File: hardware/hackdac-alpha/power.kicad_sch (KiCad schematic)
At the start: 51 parts, among them J10 HOLE, J11 HOLE, J12 HOLE, J13 HOLE, J6 EXT LEDS, J7 EXT POWER, J8 HOLE, J9 HOLE, P3 P28, P4 P20, Q7 IRLML2244, U10 74LVC1G07, U11 TPS61170DRVR, U12 TPS63700DRCT, U3 TLE2082

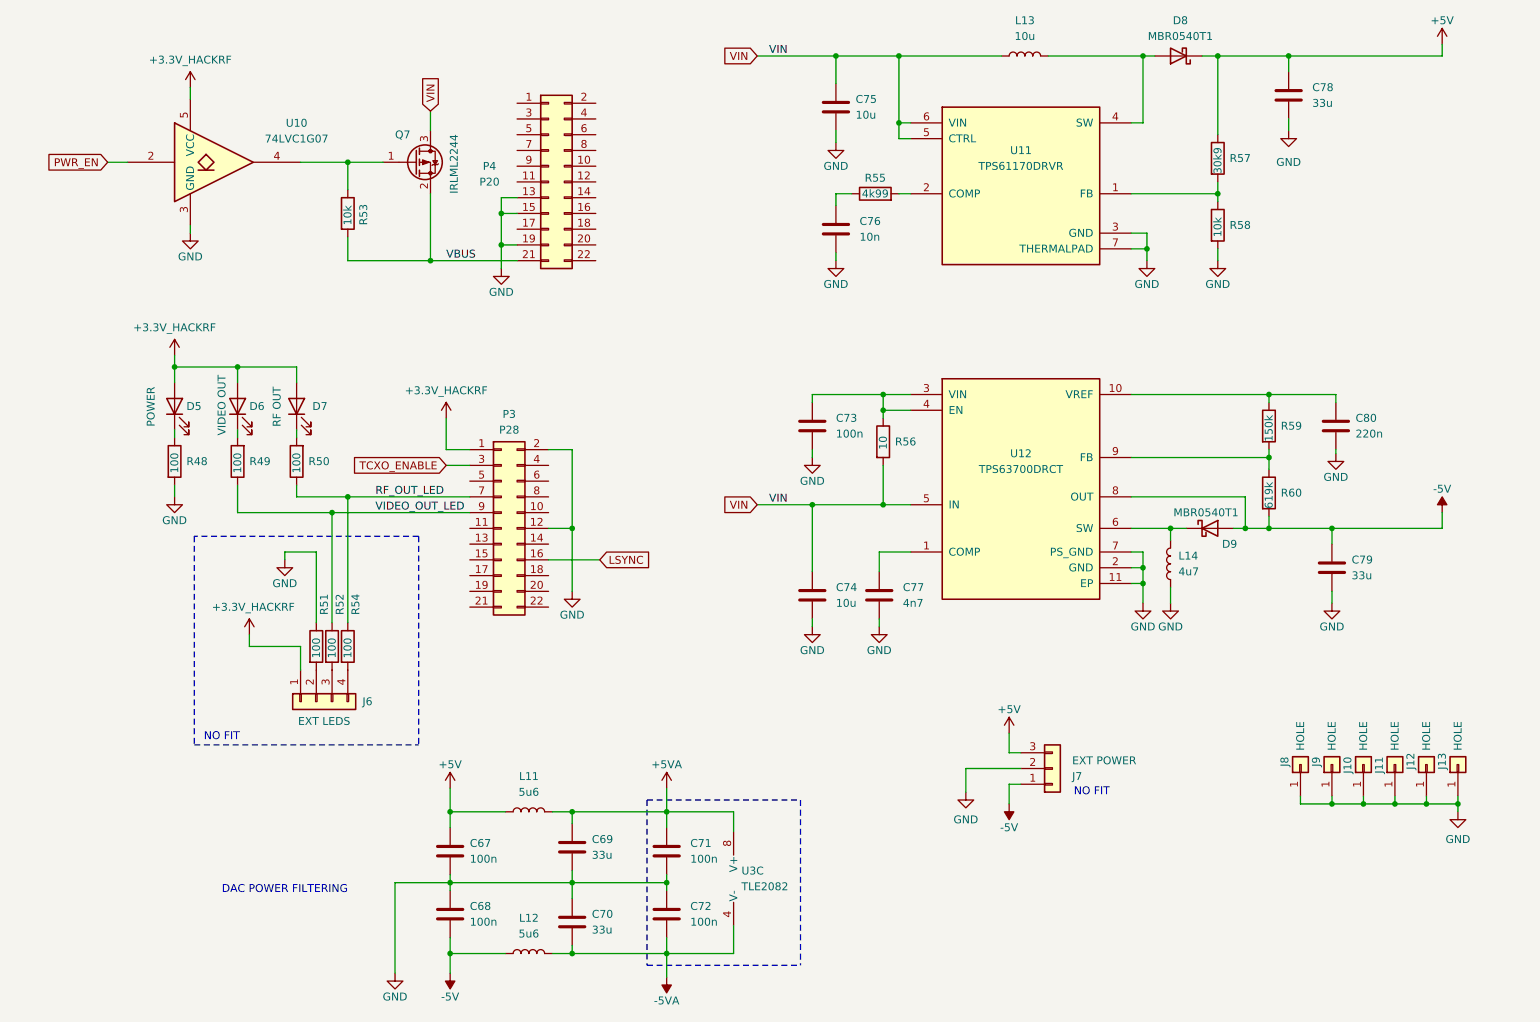
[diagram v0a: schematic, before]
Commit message: Modify I2C buffering to allow power-down of HackDAC
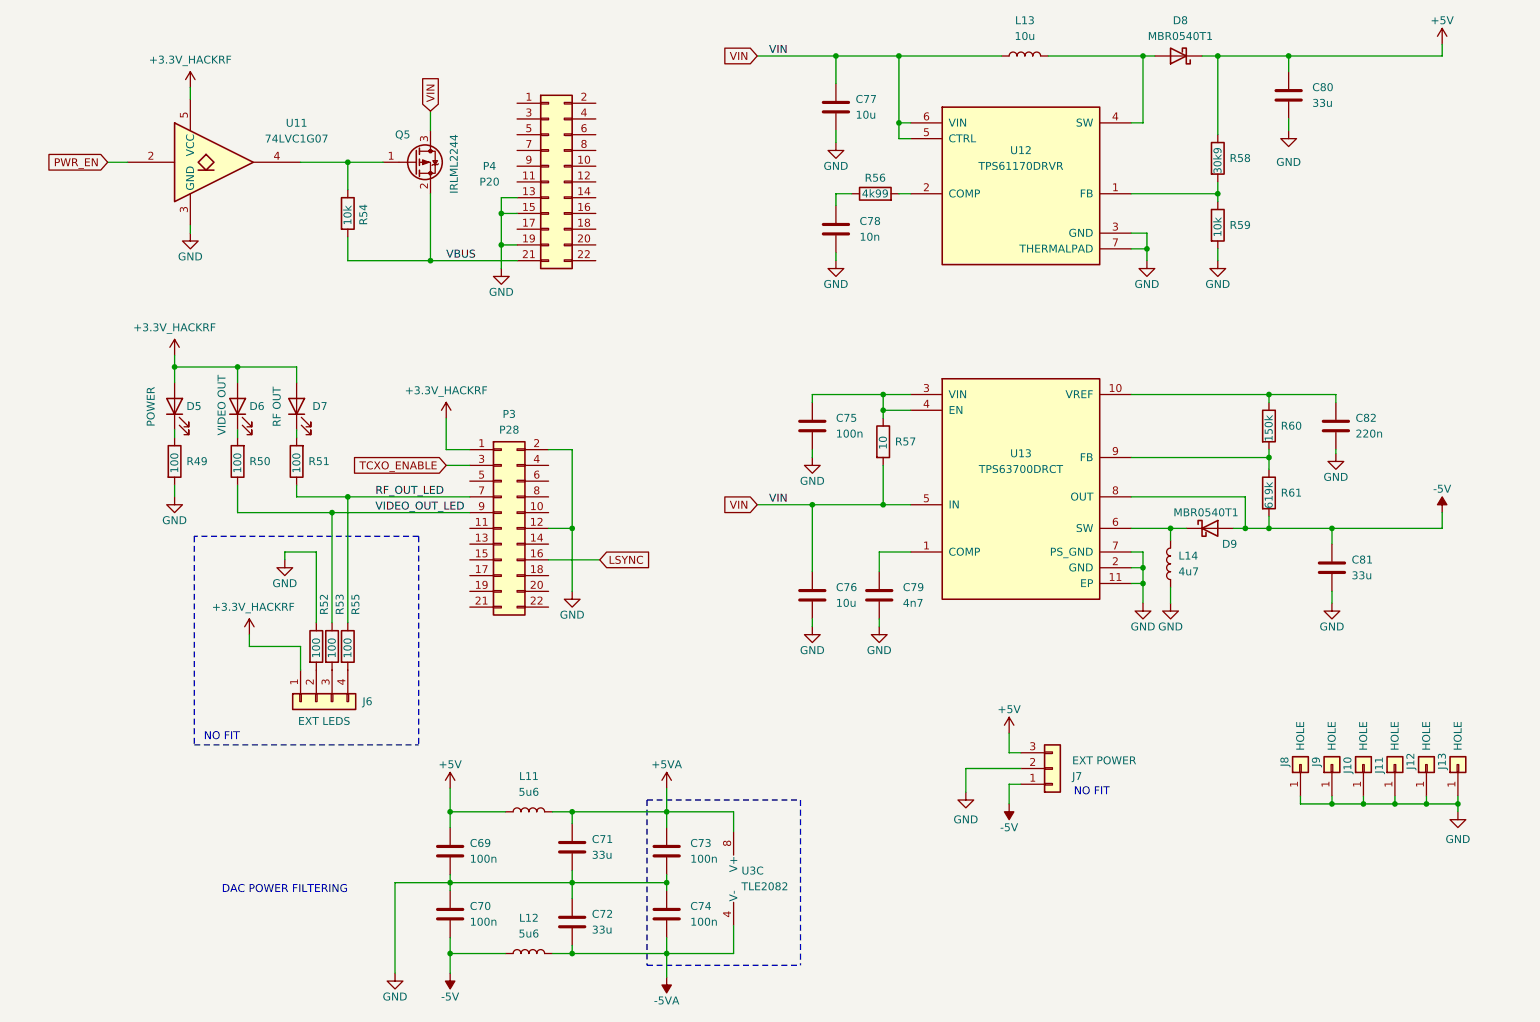
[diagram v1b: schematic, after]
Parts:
- renumbered C67 to C69, C68 to C70, C69 to C71, C70 to C72, C71 to C73, C72 to C74, C73 to C75, C74 to C76, C75 to C77, C76 to C78, C77 to C79, C78 to C80, C79 to C81, C80 to C82, Q7 to Q5, R48 to R49, R49 to R50, R50 to R51, R51 to R52, R52 to R53, R53 to R54, R54 to R55, R55 to R56, R56 to R57, R57 to R58, R58 to R59, R59 to R60, R60 to R61, U10 to U11, U11 to U12, U12 to U13

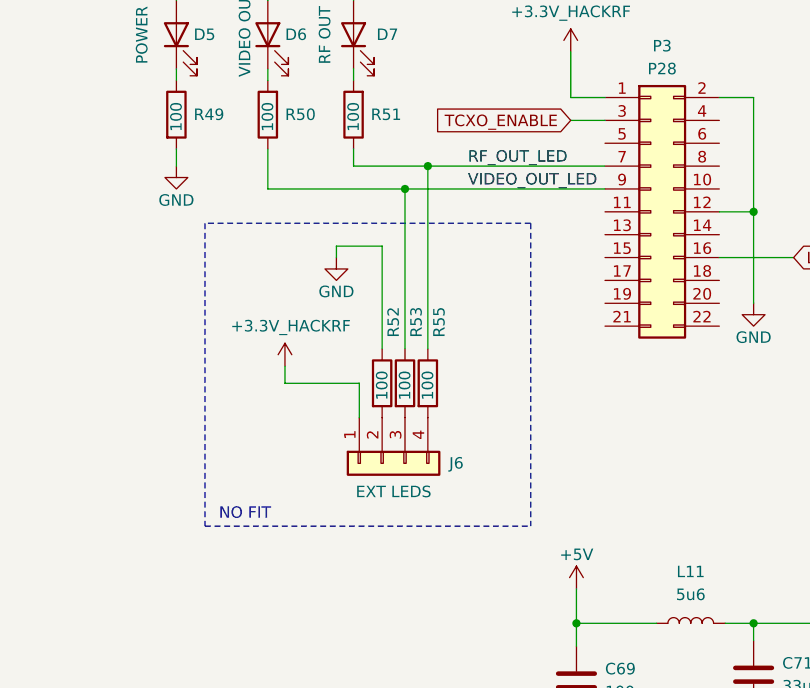
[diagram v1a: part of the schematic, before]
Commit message: Move LEDs underneath lightpipes
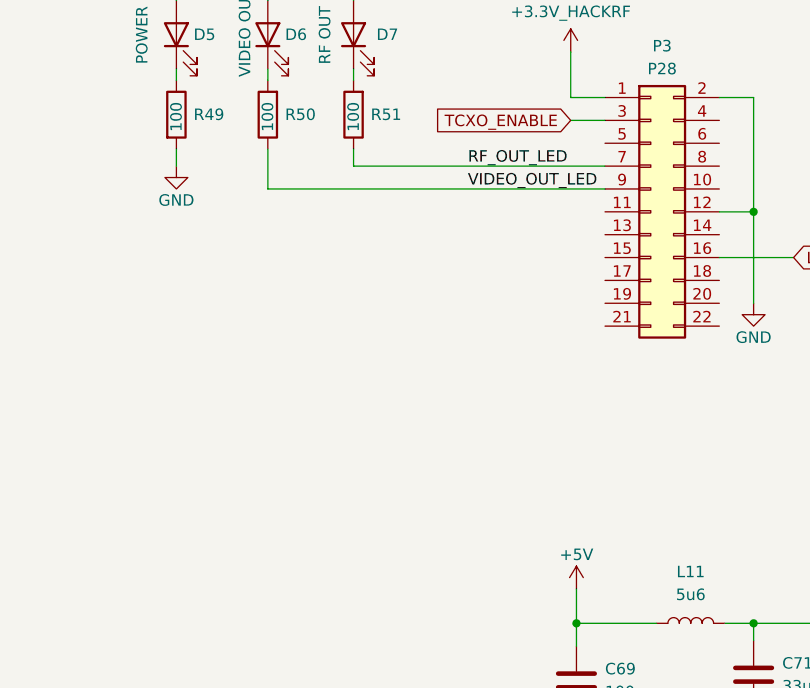
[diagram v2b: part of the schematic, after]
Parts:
- removed J6: EXT LEDS, Connector_Molex:Molex_PicoBlade_53047-0410_1x04_P1.25mm_Vertical, symbol Connector_Generic:Conn_01x04
- removed R52, R53, R55: 100, Resistor_SMD:R_0603_1608Metric, symbol Device:R

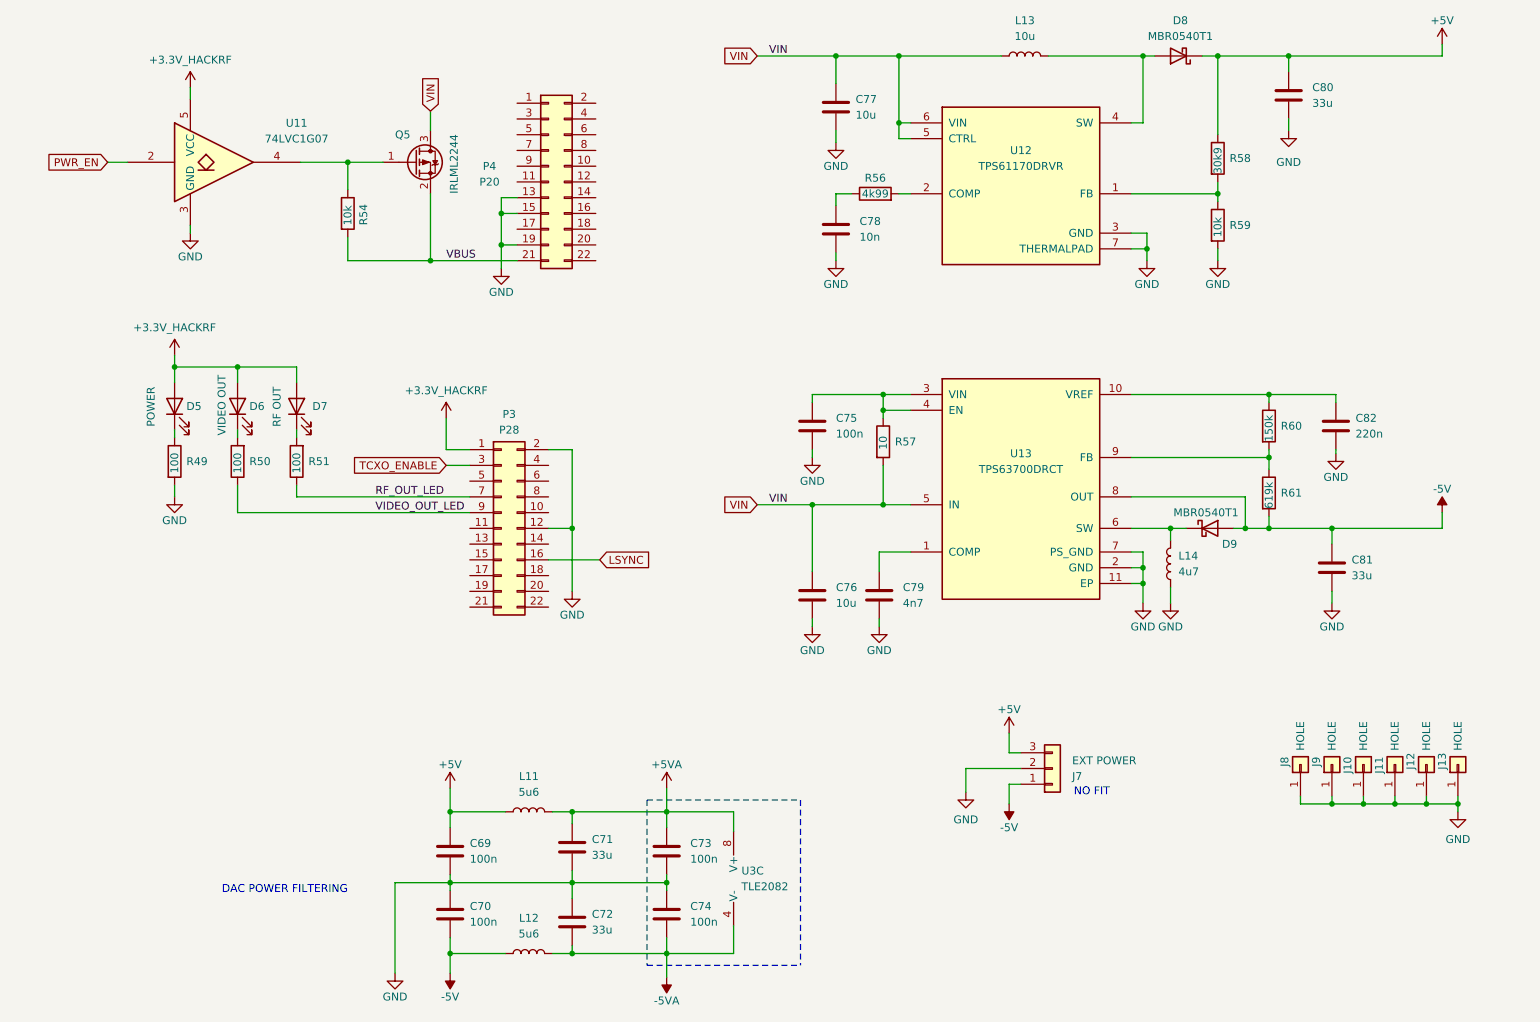
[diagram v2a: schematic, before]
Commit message: Add jumper to configure sync out connector
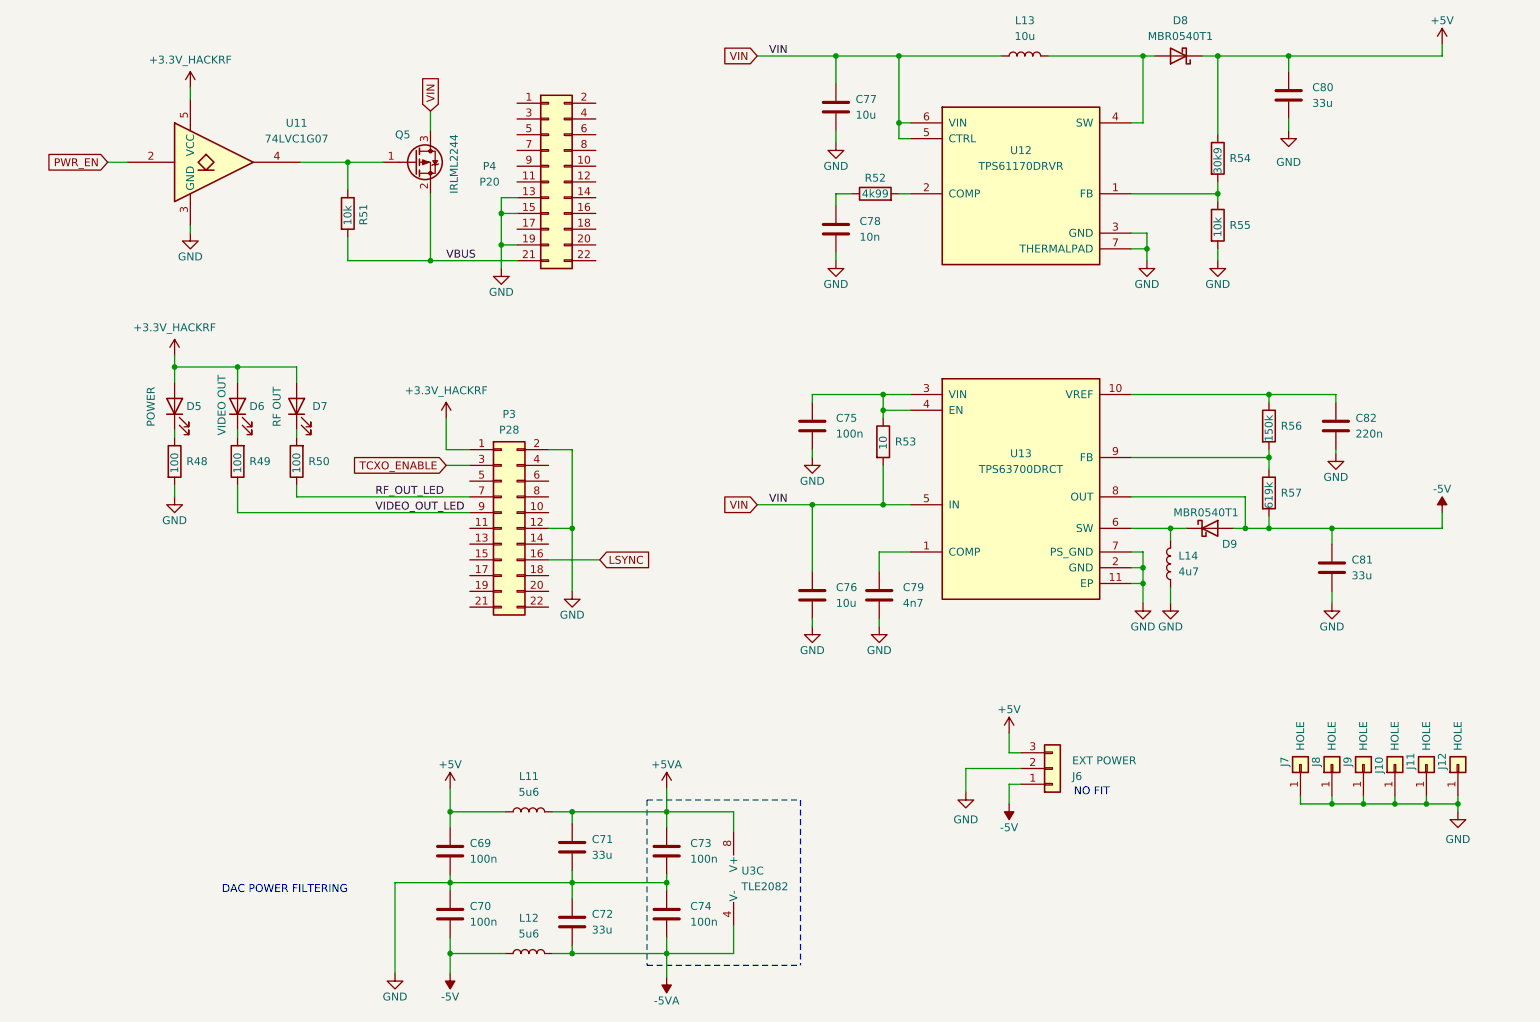
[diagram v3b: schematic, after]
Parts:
- renumbered J11 to J10, J12 to J11, J13 to J12, J7 to J6, J8 to J7, J9 to J8, J10 to J9, R49 to R48, R50 to R49, R51 to R50, R54 to R51, R56 to R52, R57 to R53, R58 to R54, R59 to R55, R60 to R56, R61 to R57

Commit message: Added configuration straps
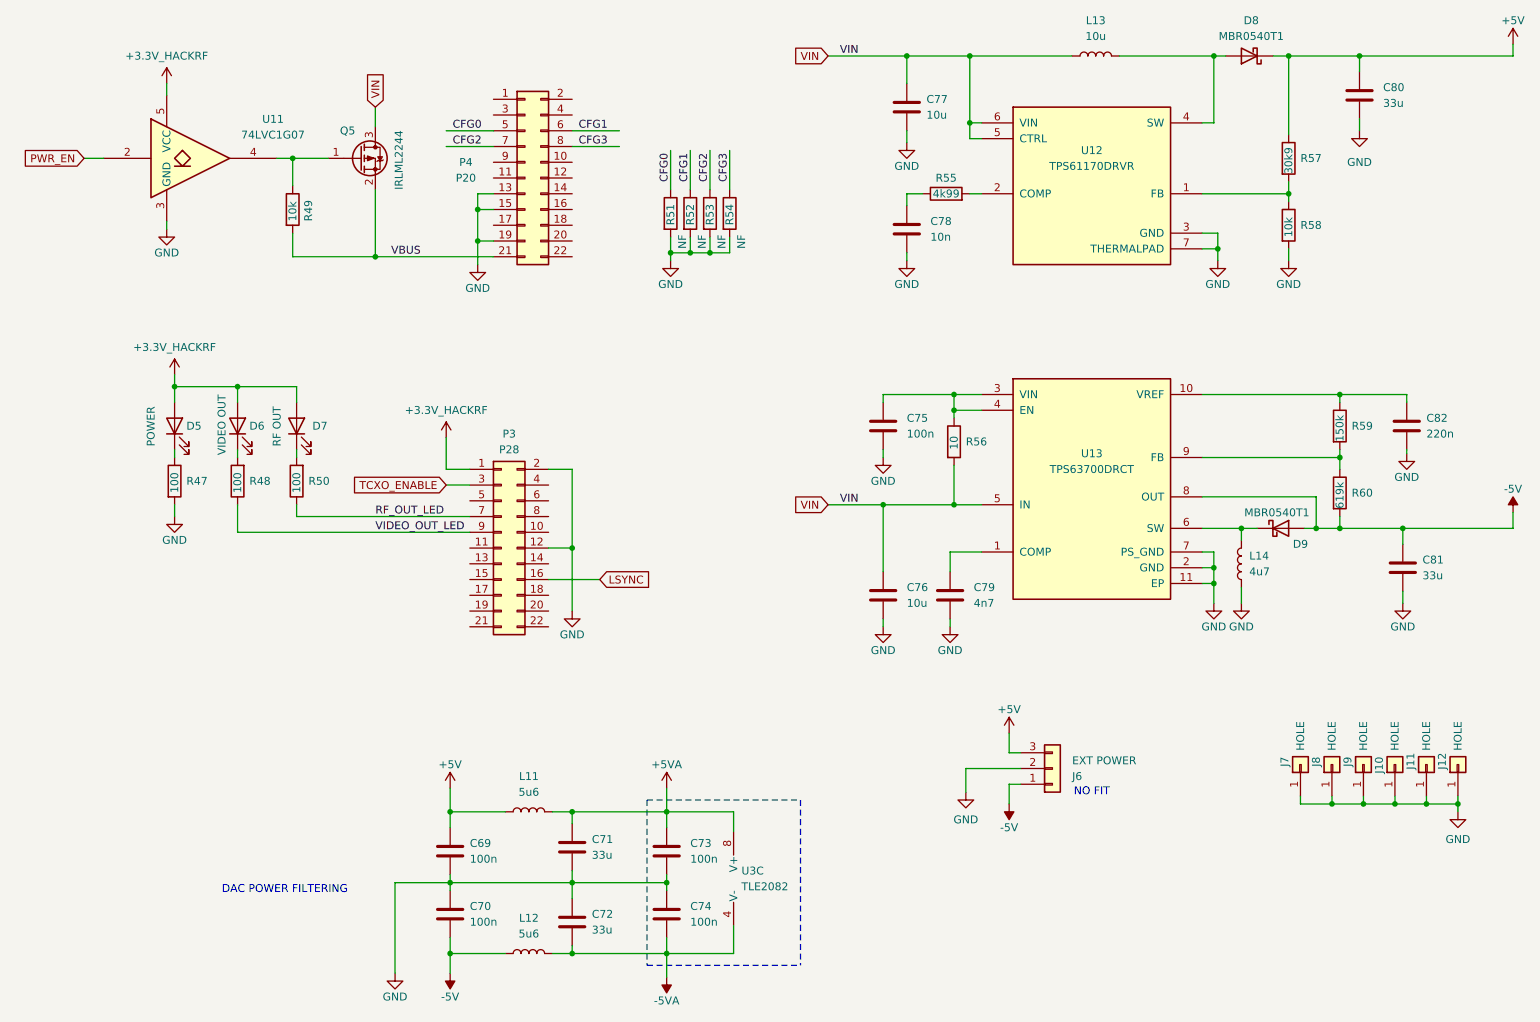
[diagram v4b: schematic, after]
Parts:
- added R51, R52, R53, R54: NF, Resistor_SMD:R_0603_1608Metric, symbol Device:R
- renumbered R48 to R47, R49 to R48, R51 to R49, R52 to R55, R53 to R56, R54 to R57, R55 to R58, R56 to R59, R57 to R60
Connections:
- net GND: now also R51.2, R52.2, R53.2, R54.2
- net CFG0: now reaches P4.5 (Pin_5)
- net CFG0: now also R51.1
- net CFG1: now reaches P4.6 (Pin_6)
- net CFG1: now also R52.1
- net CFG2: now reaches P4.7 (Pin_7)
- net CFG2: now also R53.1
- net CFG3: now reaches P4.8 (Pin_8)
- net CFG3: now also R54.1
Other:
- moved on the sheet: C75, C76, C77, C78, C79, C80, C81, C82, D5, D6, D7, D8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

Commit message: V3 tid-ups
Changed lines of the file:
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@@
 	(wire
 		(pts
-			(xy 88.9 99.06) (xy 92.71 99.06)
+			(xy 89.535 99.06) (xy 92.71 99.06)
 		)
 		(stroke
@@
 	(global_label "TCXO_ENABLE"
 		(shape input)
-		(at 88.9 99.06 180)
+		(at 89.535 99.06 180)
 		(fields_autoplaced yes)
 		(effects
@@
 		)
 		(property "Intersheetrefs" "${INTERSHEET_REFS}"
-			(at 73.1544 99.06 0)
+			(at 73.7894 99.06 0)
 			(effects
 				(font

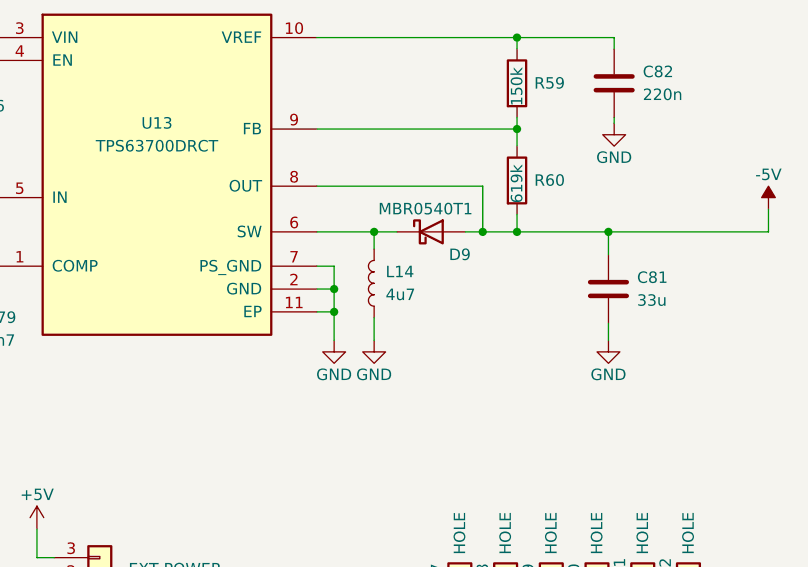
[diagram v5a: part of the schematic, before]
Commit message: Fixed a couple of incorrect component values
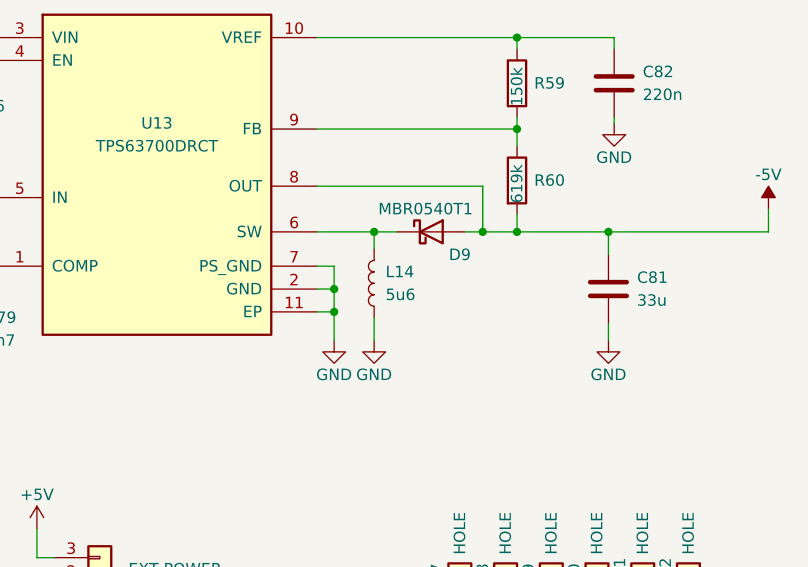
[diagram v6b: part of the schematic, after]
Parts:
- L14: value 4u7 -> 5u6
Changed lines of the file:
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@@
 		(fields_autoplaced yes)
 		(property "Reference" "L14"
-			(at 218.44 110.49 0)
+			(at 218.44 110.4899 0)
 			(effects
 				(font
@@
 			)
 		)
-		(property "Value" "4u7"
-			(at 218.44 113.03 0)
+		(property "Value" "5u6"
+			(at 218.44 113.0299 0)
 			(effects
 				(font
